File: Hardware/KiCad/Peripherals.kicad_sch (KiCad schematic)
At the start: 33 parts

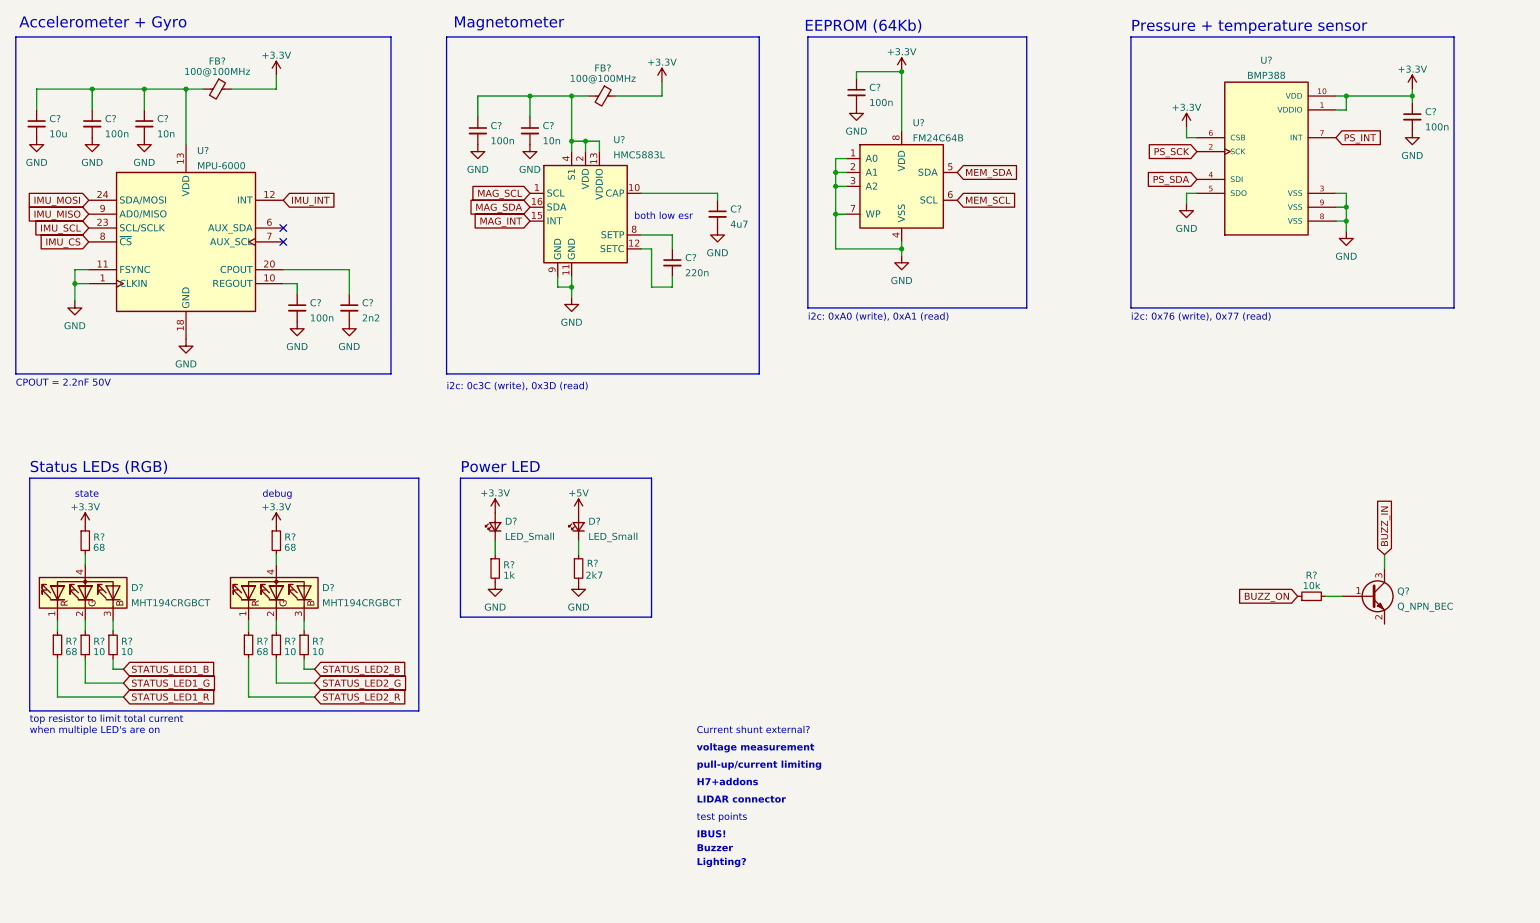
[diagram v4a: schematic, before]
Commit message: Added pinlables, added SD cardholder footprint, fixed VBUS connection, added termination resistors for high frequency signals, improved schematic layout
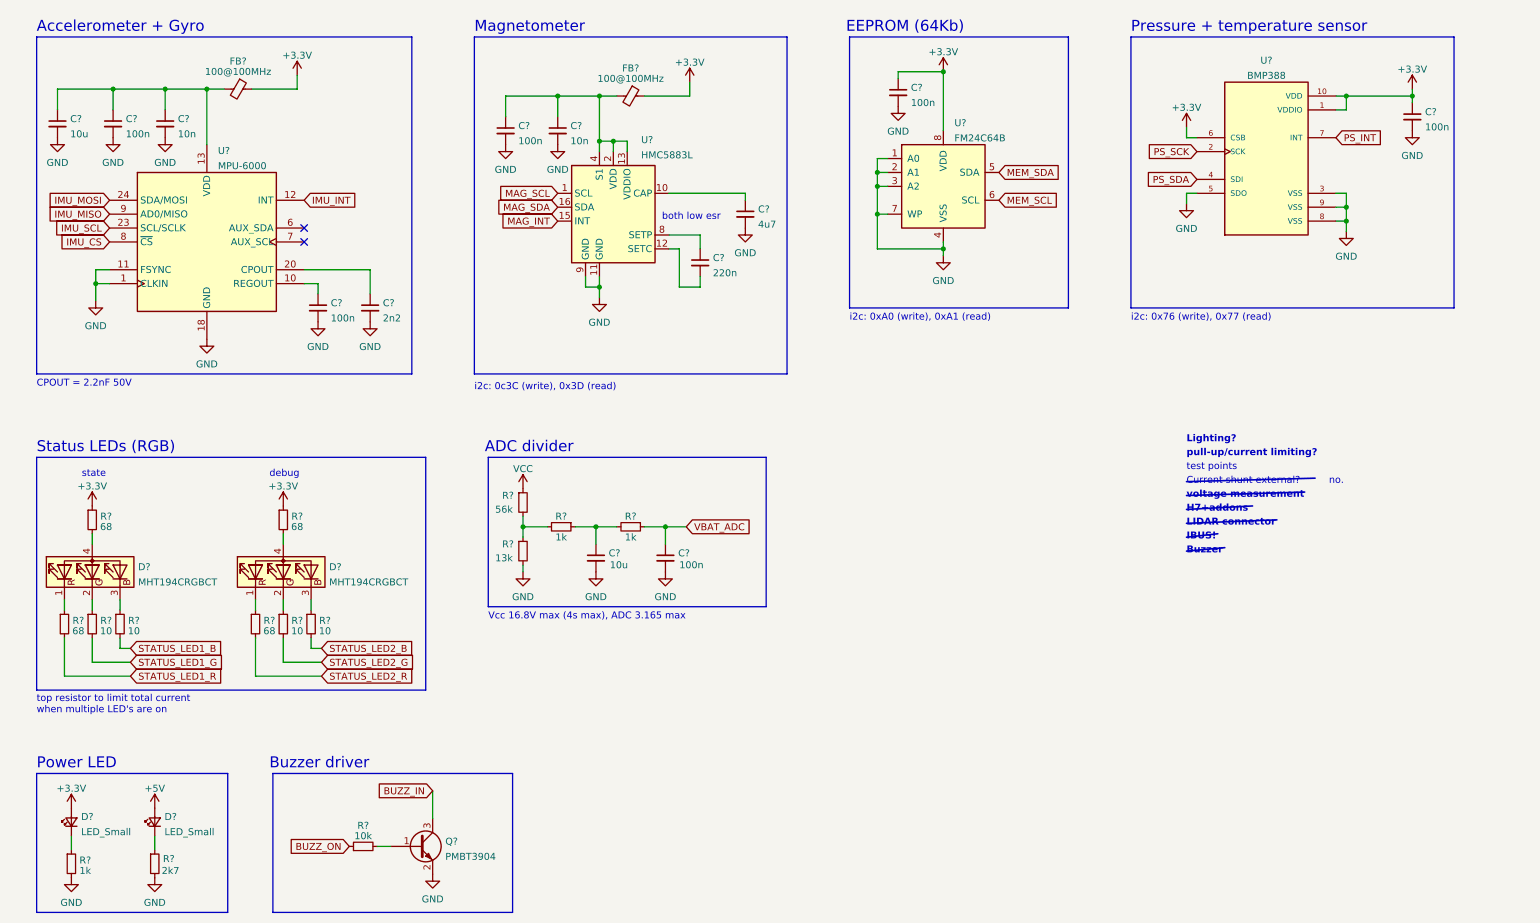
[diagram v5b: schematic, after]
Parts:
- added C?: 100n, symbol Device:C_Small
- added C?: 10u, symbol Device:C_Small
- added R? (x2): 1k, Resistor_SMD:R_0603_1608Metric, symbol Device:R_Small
- added R?: 56k, Resistor_SMD:R_0603_1608Metric, symbol Device:R_Small
- added R?: 13k, Resistor_SMD:R_0603_1608Metric, symbol Device:R_Small
- Q?: value Q_NPN_BEC -> PMBT3904; footprint (none) -> Package_TO_SOT_SMD:SOT-23
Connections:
- net GND: now also Q?.2 (E), C?.2, C?.2, R?.2
- new net: C?.1, R?.1, R?.2
- new net: R?.1, R?.2, R?.2
- new net VBAT_ADC: C?.1, R?.1
- new net VCC: R?.1
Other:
- note added: "ADC divider"
- note added: "Buzzer driver"
- note added: "Vcc 16.8V max (4s max), ADC 3.165 max"
- note added: "no."
- note added: "pull-up/current limiting?"
- note removed: "pull-up/current limiting"
- moved on the sheet: C?, D?, FB?, Q?, R?, U?

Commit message: Added pullups, testpoints and more pin definitions
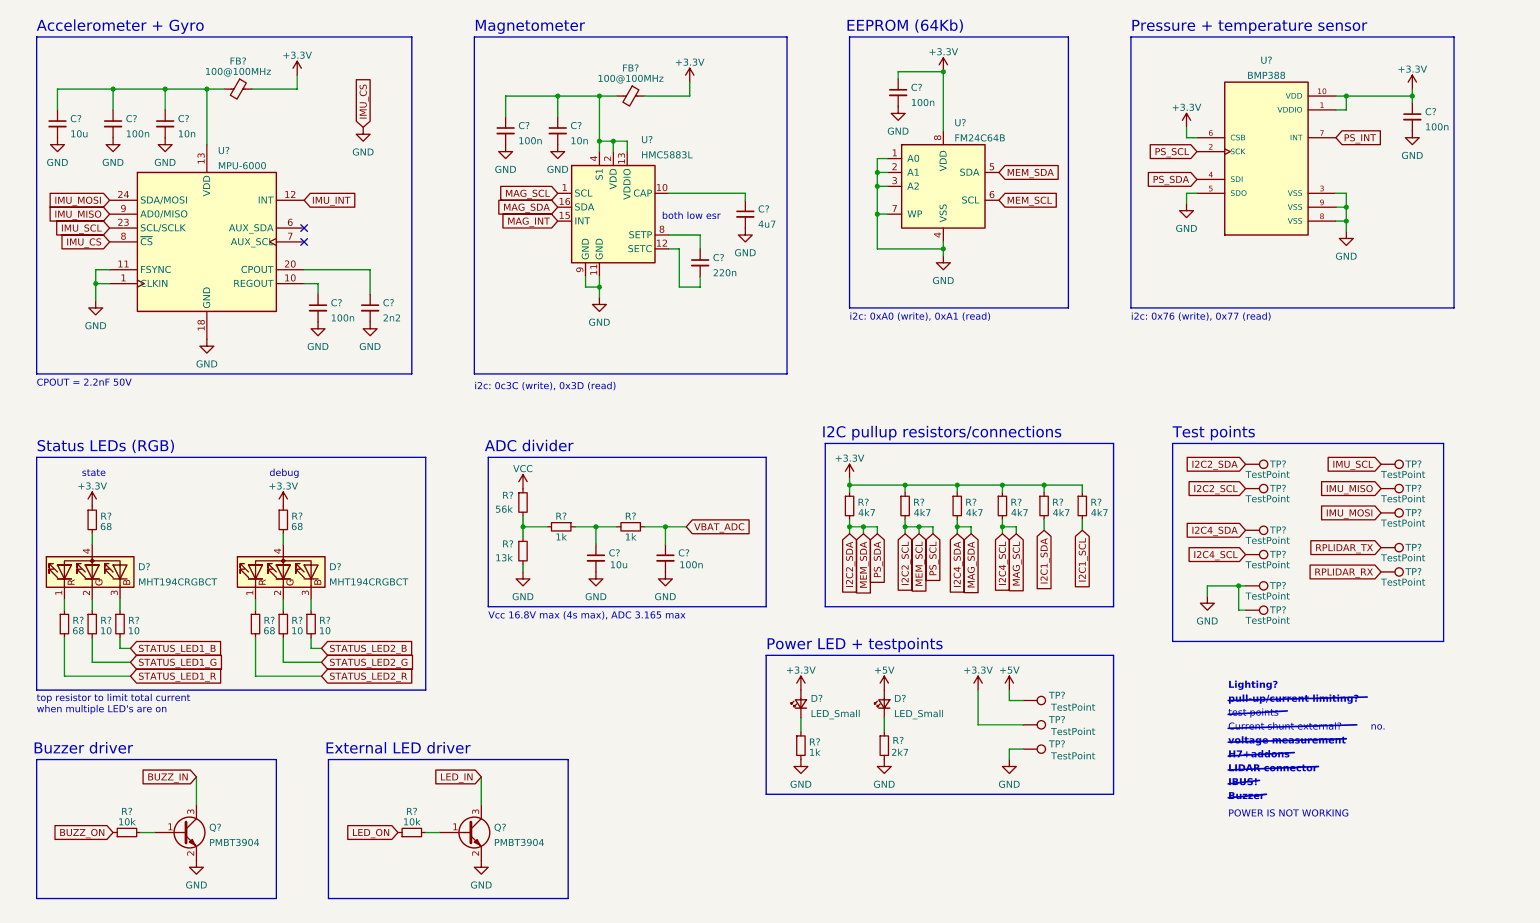
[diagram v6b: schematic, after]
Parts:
- added Q?: PMBT3904, Package_TO_SOT_SMD:SOT-23, symbol Device:Q_NPN_BEC
- added R?: 10k, symbol Device:R_Small
- added R? (x6): 4k7, Resistor_SMD:R_0603_1608Metric, symbol Device:R_Small
- added TP? (x14): TestPoint, symbol Connector:TestPoint
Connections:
- net IMU_CS is gone; now on net GND: U?.8 (~{CS})
- net PS_SCK is gone; now on net I2C2_SCL: U?.2 (SCK)
- net PS_SDA is gone; now on net I2C2_SDA: U?.4 (SDI)
- net +3V3: now also R?.1, R?.1, R?.1, R?.1, R?.1, R?.1, TP?.1
- net +5V: now also TP?.1
- net GND: now also Q?.2 (E), TP?.1, TP?.1, TP?.1
- net IMU_MISO: now also TP?.1
- net IMU_MOSI: now also TP?.1
- net IMU_SCL: now also TP?.1
- net MAG_SCL renamed I2C4_SCL
- net I2C4_SCL: now also R?.2, TP?.1
- net MAG_SDA renamed I2C4_SDA
- net I2C4_SDA: now also R?.2, TP?.1
- net MEM_SCL renamed I2C2_SCL
- net I2C2_SCL: now also R?.2, TP?.1
- net MEM_SDA renamed I2C2_SDA
- net I2C2_SDA: now also R?.2, TP?.1
- new net: Q?.1 (B), R?.2
- new net I2C1_SCL: R?.2
- new net I2C1_SDA: R?.2
- new net LED_IN: Q?.3 (C)
- new net LED_ON: R?.1
- new net RPLIDAR_RX: TP?.1
- new net RPLIDAR_TX: TP?.1
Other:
- note added: "External LED driver"
- note added: "I2C pullup resistors/connections"
- note added: "POWER IS NOT WORKING"
- note added: "Power LED + testpoints"
- note added: "Test points"
- note removed: "Power LED"
- moved on the sheet: D?, Q?, R?

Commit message: Switched some RX and TX pins
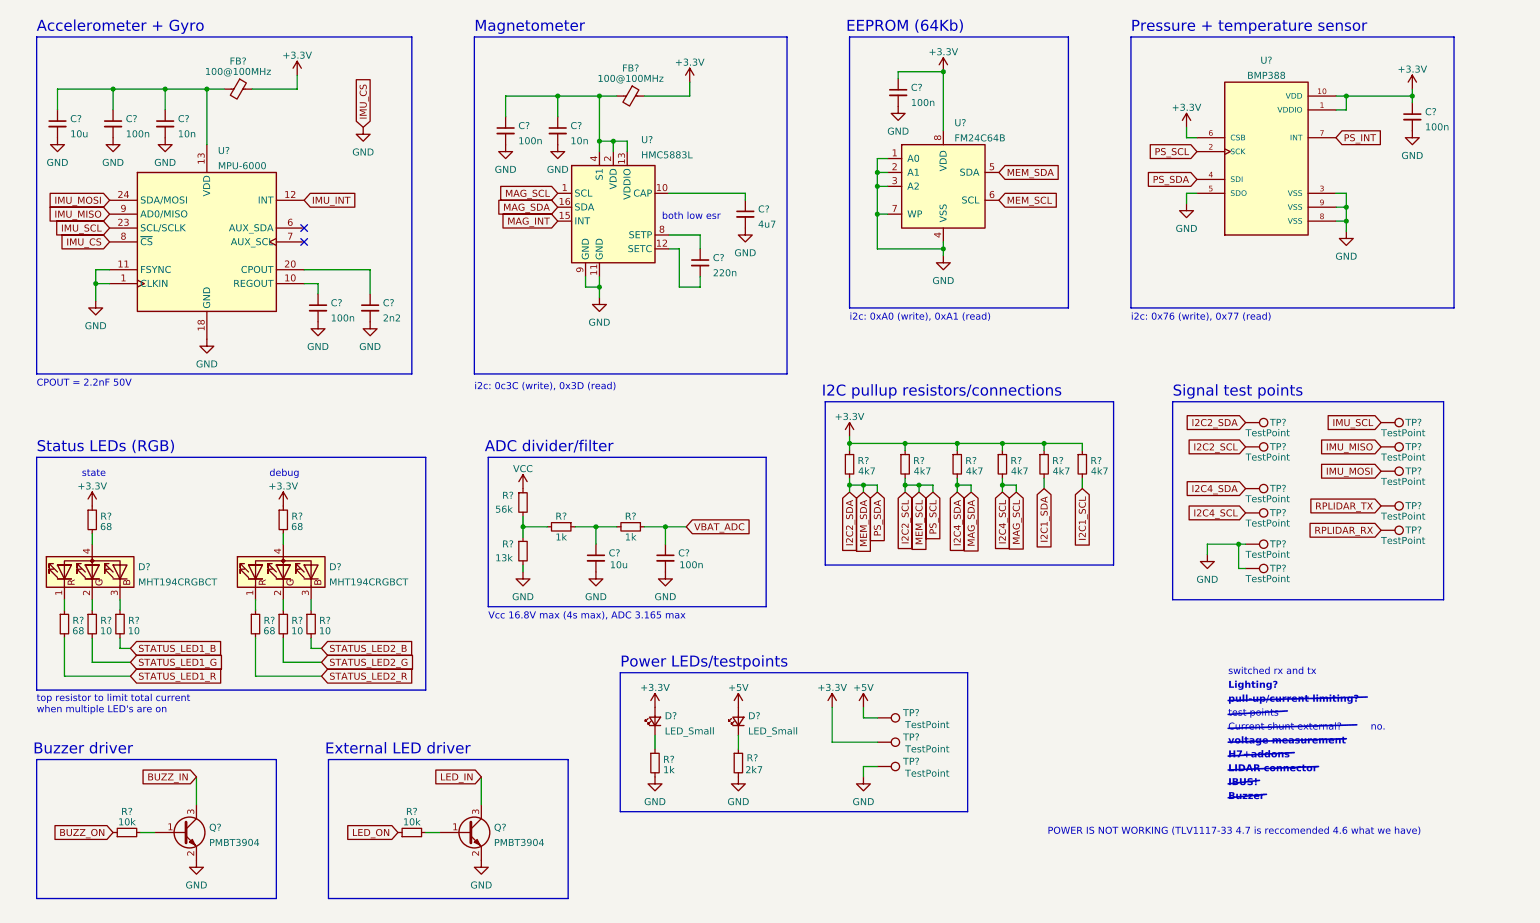
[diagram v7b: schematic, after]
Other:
- note added: "ADC divider/filter"
- note added: "POWER IS NOT WORKING (TLV1117-33 4.7 is reccomended 4.6 what we have)"
- note added: "Power LEDs/testpoints"
- note added: "Signal test points"
- note added: "switched rx and tx"
- note removed: "ADC divider"
- note removed: "POWER IS NOT WORKING"
- note removed: "Power LED + testpoints"
- note removed: "Test points"
- moved on the sheet: D?, R?, TP?
